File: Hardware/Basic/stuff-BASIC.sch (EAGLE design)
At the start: 52 parts, among them SW1 SWITCH.MOM, SW2 SWITCH.MOM, SW5 SWITCH.MOM, U2 NRF52832_MODULE_MDBT42, U4 PCF8523

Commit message: done until 22 min mark
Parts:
- removed SW5: SWITCH.MOM, LinnesLab-Switches:SWITCH.MOM
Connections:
- removed net N$16: SW1.3, SW1.4
- removed net N$18: SW1.1
- removed net VBATT: U4.VBAT
- new net SW1: SW1.1, SW2.1
- net GND: now also SW1.3, SW1.4, SW2.3, SW2.4
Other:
- note added: "Buttons"
- note added: "Cortex Debugger/ Programmer"
- note added: "Power Management"
- note added: "RTC"
- note added: "Real-Time Clock"
- note added: "SD Card"
- note added: "nRFS2832 M"
- moved on the sheet: C13, C15, C16, C17, C18, C19, C20, C21, C5, C6, CHRG2, D4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

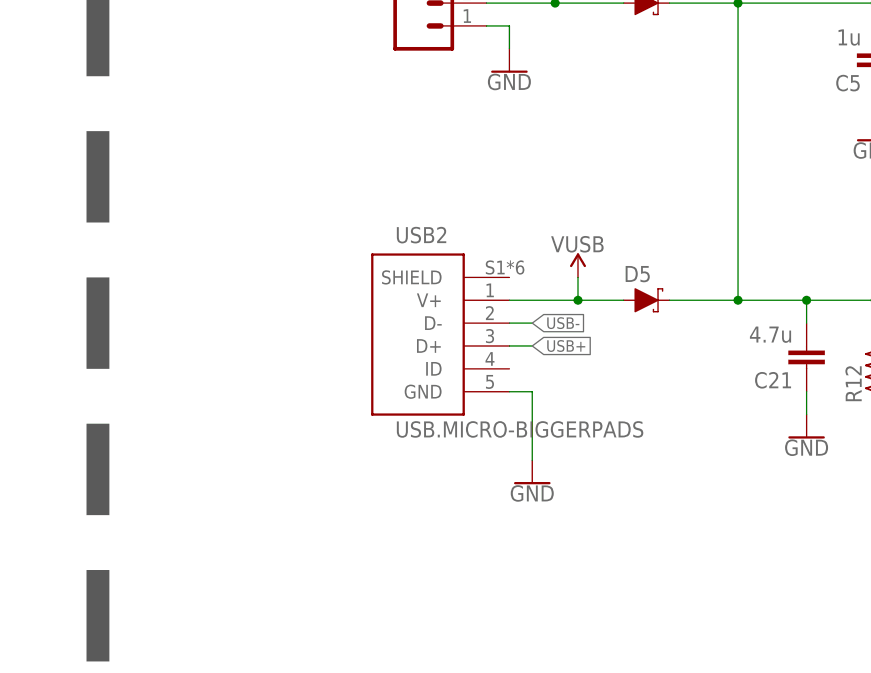
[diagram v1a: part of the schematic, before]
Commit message: Complete arduino video and add header
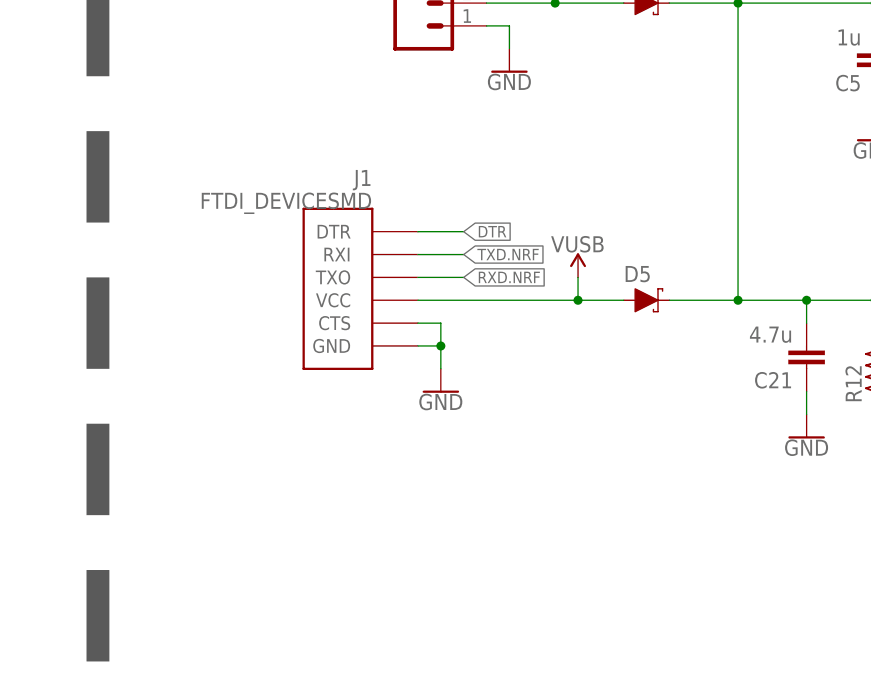
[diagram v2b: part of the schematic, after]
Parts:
- removed USB2: USB.MICRO-BIGGERPADS, LinnesLab-Connectors:USB.MICRO-BIGGERPADS
- added J1: FTDI_DEVICESMD, LinnesLab-Connectors:FTDI_DEVICESMD
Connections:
- removed net USB+: USB2.D+
- removed net USB-: USB2.D-
- new net RXD.NRF: J1.TXO
- new net TXD.NRF: J1.RXI
- net DTR: now also J1.DTR
- net GND: now also J1.CTS, J1.GND; no longer USB2.GND
- net V_USB: now also J1.VCC; no longer USB2.V+
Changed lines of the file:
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@@
 <part name="D4" library="LinnesLab-DiscreteSemi" deviceset="SCHOTTKY" device="-USC" package3d_urn="urn:adsk.eagle:package:15664784/2"/>
 <part name="D5" library="LinnesLab-DiscreteSemi" deviceset="SCHOTTKY" device="-USC" package3d_urn="urn:adsk.eagle:package:15664784/2"/>
-<part name="USB2" library="LinnesLab-Connectors" deviceset="USB.MICRO" device="-BIGGERPADS"/>
 <part name="J2" library="LinnesLab-Connectors" deviceset="CONN_02" device=""/>
 <part name="C5" library="LinnesLab-Passives" deviceset="CAPACITOR" device="0603" package3d_urn="urn:adsk.eagle:package:15661989/2" value="1u"/>
@@
 <part name="GND38" library="LinnesLab-Symbols" deviceset="GND" device=""/>
 <part name="GND39" library="LinnesLab-Symbols" deviceset="GND" device=""/>
-<part name="GND40" library="LinnesLab-Symbols" deviceset="GND" device=""/>
 <part name="GND41" library="LinnesLab-Symbols" deviceset="GND" device=""/>
 <part name="SUPPLY12" library="LinnesLab-Symbols" deviceset="3.3V" device=""/>
@@
 <part name="SW2" library="LinnesLab-Switches" deviceset="SWITCH.MOM" device=""/>
 <part name="GND2" library="LinnesLab-Symbols" deviceset="GND" device=""/>
+<part name="J1" library="LinnesLab-Connectors" deviceset="FTDI_DEVICE" device="SMD"/>
+<part name="GND6" library="LinnesLab-Symbols" deviceset="GND" device=""/>
 </parts>
 <sheets>
@@
 <attribute name="VALUE" x="30.48" y="-68.072" size="1.778" layer="96" font="vector" align="top-left"/>
 </instance>
-<instance part="USB2" gate="G$1" x="10.16" y="-71.12" smashed="yes">
-<attribute name="NAME" x="5.08" y="-59.69" size="1.778" layer="95"/>
-<attribute name="VALUE" x="5.08" y="-81.28" size="1.778" layer="96"/>
-</instance>
 <instance part="J2" gate="G$1" x="7.62" y="-35.56" smashed="yes">
 <attribute name="VALUE" x="5.08" y="-40.386" size="1.778" layer="96" font="vector"/>
@@
 <instance part="GND39" gate="G$1" x="50.8" y="-81.28" smashed="yes">
 <attribute name="VALUE" x="50.8" y="-81.534" size="1.778" layer="96" align="top-center"/>
-</instance>
-<instance part="GND40" gate="G$1" x="20.32" y="-86.36" smashed="yes">
-<attribute name="VALUE" x="20.32" y="-86.614" size="1.778" layer="96" align="top-center"/>
 </instance>
 <instance part="GND41" gate="G$1" x="17.78" y="-40.64" smashed="yes">
@@
 <instance part="GND2" gate="G$1" x="213.36" y="-40.64" smashed="yes">
 <attribute name="VALUE" x="213.36" y="-40.894" size="1.778" layer="96" align="top-center"/>
+</instance>
+<instance part="J1" gate="G$1" x="2.54" y="-63.5" smashed="yes" rot="MR0">
+<attribute name="NAME" x="2.54" y="-53.34" size="1.778" layer="95" rot="MR0"/>
+<attribute name="VALUE" x="2.54" y="-55.88" size="1.778" layer="96" rot="MR0"/>
+</instance>
+<instance part="GND6" gate="G$1" x="10.16" y="-76.2" smashed="yes">
+<attribute name="VALUE" x="10.16" y="-76.454" size="1.778" layer="96" align="top-center"/>
 </instance>
 </instances>
@@
 </segment>
 <segment>
-<pinref part="USB2" gate="G$1" pin="GND"/>
-<wire x1="17.78" y1="-76.2" x2="20.32" y2="-76.2" width="0.1524" layer="91"/>
-<pinref part="GND40" gate="G$1" pin="GND"/>
-<wire x1="20.32" y1="-76.2" x2="20.32" y2="-83.82" width="0.1524" layer="91"/>
-</segment>
-<segment>
 <pinref part="J2" gate="G$1" pin="1"/>
 <wire x1="15.24" y1="-35.56" x2="17.78" y2="-35.56" width="0.1524" layer="91"/>
@@
 <junction x="213.36" y="-30.48"/>
 <pinref part="GND2" gate="G$1" pin="GND"/>
+</segment>
+<segment>
+<pinref part="J1" gate="G$1" pin="GND"/>
+<pinref part="GND6" gate="G$1" pin="GND"/>
+<wire x1="7.62" y1="-71.12" x2="10.16" y2="-71.12" width="0.1524" layer="91"/>
+<wire x1="10.16" y1="-71.12" x2="10.16" y2="-73.66" width="0.1524" layer="91"/>
+<pinref part="J1" gate="G$1" pin="CTS"/>
+<wire x1="7.62" y1="-68.58" x2="10.16" y2="-68.58" width="0.1524" layer="91"/>
+<wire x1="10.16" y1="-71.12" x2="10.16" y2="-68.58" width="0.1524" layer="91"/>
+<junction x="10.16" y="-71.12"/>
 </segment>
 </net>
@@
 <label x="55.88" y="83.82" size="1.27" layer="95" rot="R180" xref="yes"/>
 </segment>
+<segment>
+<pinref part="J1" gate="G$1" pin="DTR"/>
+<wire x1="7.62" y1="-58.42" x2="12.7" y2="-58.42" width="0.1524" layer="91"/>
+<label x="12.7" y="-58.42" size="1.27" layer="95" xref="yes"/>
+</segment>
 </net>
 <net name="P0.10/NFC2" class="0">
@@
 <net name="V_USB" class="0">
 <segment>
-<pinref part="USB2" gate="G$1" pin="V+"/>
 <pinref part="D5" gate="G$1" pin="A"/>
 <wire x1="30.48" y1="-66.04" x2="25.4" y2="-66.04" width="0.1524" layer="91"/>
 <pinref part="SUPPLY13" gate="G$1" pin="V_USB"/>
-<wire x1="25.4" y1="-66.04" x2="17.78" y2="-66.04" width="0.1524" layer="91"/>
 <wire x1="25.4" y1="-63.5" x2="25.4" y2="-66.04" width="0.1524" layer="91"/>
+<pinref part="J1" gate="G$1" pin="VCC"/>
+<wire x1="7.62" y1="-66.04" x2="25.4" y2="-66.04" width="0.1524" layer="91"/>
 <junction x="25.4" y="-66.04"/>
 </segment>
@@
 <wire x1="63.5" y1="-71.12" x2="66.04" y2="-71.12" width="0.1524" layer="91"/>
 <label x="63.5" y="-83.82" size="1.27" layer="95" xref="yes"/>
-</segment>
-</net>
-<net name="USB-" class="0">
-<segment>
-<pinref part="USB2" gate="G$1" pin="D-"/>
-<wire x1="17.78" y1="-68.58" x2="20.32" y2="-68.58" width="0.1524" layer="91"/>
-<label x="20.32" y="-68.58" size="1.27" layer="95" xref="yes"/>
-</segment>
-</net>
-<net name="USB+" class="0">
-<segment>
-<pinref part="USB2" gate="G$1" pin="D+"/>
-<wire x1="17.78" y1="-71.12" x2="20.32" y2="-71.12" width="0.1524" layer="91"/>
-<label x="20.32" y="-71.12" size="1.27" layer="95" xref="yes"/>
 </segment>
 </net>
@@
 </segment>
 </net>
+<net name="TXD.NRF" class="0">
+<segment>
+<pinref part="J1" gate="G$1" pin="RXI"/>
+<wire x1="7.62" y1="-60.96" x2="12.7" y2="-60.96" width="0.1524" layer="91"/>
+<label x="12.7" y="-60.96" size="1.27" layer="95" xref="yes"/>
+</segment>
+</net>
+<net name="RXD.NRF" class="0">
+<segment>
+<pinref part="J1" gate="G$1" pin="TXO"/>
+<wire x1="7.62" y1="-63.5" x2="12.7" y2="-63.5" width="0.1524" layer="91"/>
+<label x="12.7" y="-63.5" size="1.27" layer="95" xref="yes"/>
+</segment>
+</net>

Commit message: Complete schematic
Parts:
- removed C10, C11: 300p, LinnesLab-Passives:CAPACITOR0603
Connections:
- removed net RXD: U2.P0.08
- removed net TXD: U2.P0.06
- new net A4/PPG: U2.P0.28/AIN4
- new net A5/TIA: U2.P0.29/AIN5
- new net A7/BATT: U2.P0.31/AIN7
- new net D11/SW1: U2.P0.11
- new net D15/SW2: U2.P0.15
- new net D16/CS.OLED: U2.P0.16
- new net D27/CHRG.STATUS: U2.P0.27
- new net D3/RESET.OLED: U2.P0.03/AIN1
- new net D30/LED.CNTRL: U2.P0.30/AIN6
- new net D4/DC.OLED: U2.P0.04/AIN2
- new net D5/CD1: U2.P0.05/AIN3
- new net D7/SD.CS: U2.P0.07
- net GND: no longer C10.2, C11.2
- net P0.09/NFC1: no longer C11.1
- net P0.10/NFC2: no longer C10.1
- net RXD.NRF: now also U2.P0.08
- net TXD.NRF: now also U2.P0.06
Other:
- moved on the sheet: J1, SW1, SW2

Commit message: Start organizing and routing
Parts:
- removed SD3: (no value), LinnesLab-Connectors:MICROSD
- added J3: (no value), LinnesLab-Connectors:CONN_07-1.27MM
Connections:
- removed net BATT: R13.1, R14.2
- removed net CD1: SD3.CARD_DETECT
- removed net CD2: SD3.CARD_DETECT1
- removed net CHRG.STAT: CHRG2.STAT, R12.1
- removed net CS.OLED: U3./CS
- removed net D30/LED.CNTRL: U2.P0.30/AIN6
- removed net DC.OLED: U3.DC/I2C_SA0
- removed net RESET.OLED: U3./RES
- removed net SD.CS: SD3.CS
- removed net SW1: SW1.1, SW2.1
- new net D30/LED.CTRL: J3.5, U2.P0.30/AIN6
- new net N$16: J3.4
- new net VBATT: U4.VBAT
- net 3.3V: no longer SD3.VDD
- net A4/PPG: now also J3.7
- net A5/TIA: now also J3.6
- net A7/BATT: now also R13.1, R14.2
- net D11/SW1: now also SW1.1
- net D15/SW2: now also SW2.1
- net D16/CS.OLED: now also U3./CS
- net D27/CHRG.STATUS: now also CHRG2.STAT, R12.1
- net D3/RESET.OLED: now also U3./RES
- net D4/DC.OLED: now also U3.DC/I2C_SA0
- net GND: now also J3.3; no longer SD3.GND, SD3.GND1, SD3.VSS
- net MISO: no longer SD3.DATA_OUT
- net MOSI: no longer SD3.DATA_IN
- net SCK: no longer SD3.SCLK
- net SCL: now also J3.2
- net SDA: now also J3.1
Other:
- note added: "Headers connecting top and bottom boards"
- note removed: "Connect MISO, MOSI, and SCK to appropriate pins on microcontroller. Those are SPI pins and are generally prespecified. You have more flexibility with the SD.CS pin."
- note removed: "SD Card"
- moved on the sheet: SW2

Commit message: Airwires
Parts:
- removed C2: 1u, LinnesLab-Passives:CAPACITOR0603
- removed R15: 100k, LinnesLab-Passives:RESISTOR0603
- removed U4: PCF8523, LinnesLab-Clocks:PCF8523
- removed XTAL3: 32.7680kHz, LinnesLab-Clocks:CRYSTALECS-.327-12.5-12-C-TR
- added C3: 1u, LinnesLab-Passives:CAPACITOR0603
- added U5: PCF8523, LinnesLab-Clocks:PCF8523
- added XTAL4: 32.7680kHz, LinnesLab-Clocks:CRYSTALECS-.327-12.5-12-C-TR
- C13, C15, C17, C18, C19: device LinnesLab-Passives:CAPACITOR0402 -> LinnesLab-Passives:CAPACITOR0603
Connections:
- removed net N$16: J3.4
- removed net N$19: U4.OSCO, XTAL3.1
- removed net N$20: U4.OSCI, XTAL3.2
- new net N$21: U5.OSCO, XTAL4.1
- new net N$22: U5.OSCI, XTAL4.2
- net 3.3V: now also C3.1, J3.4, U5.VDD; no longer C2.1, R15.2, U4.VDD
- net GND: now also C3.2, U5.VSS; no longer C2.2, R15.1, SW1.3, SW2.3, U4.VSS
- net SCL: now also U5.SCL; no longer U4.SCL
- net SDA: now also U5.SDA; no longer U4.SDA
- net VBATT: now also U5.VBAT; no longer U4.VBAT
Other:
- note added: "Cortex Debugger"
- note added: "Headers connecting top and bottom board"
- note removed: "Cortex Debugger/ Programmer"
- note removed: "Headers connecting top and bottom boards"
- moved on the sheet: C12, C13, C14, C15, C16, C17, C18, C19, C20, C21, C5, C6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
